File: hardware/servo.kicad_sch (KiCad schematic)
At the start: 3 parts, among them J701 Conn_02x03_Odd_Even

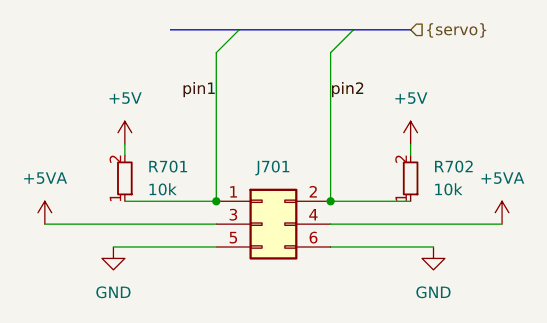
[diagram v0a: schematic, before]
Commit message: update board file, made similar to OS solenoid decoder
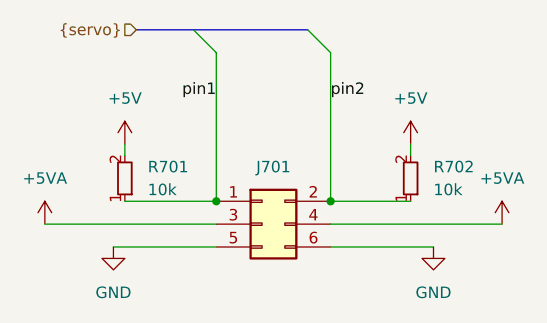
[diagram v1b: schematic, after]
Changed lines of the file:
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@@
 	)
 	(bus_entry
-		(at 149.86 69.85)
-		(size -2.54 2.54)
+		(at 132.08 69.85)
+		(size 2.54 2.54)
 		(stroke
 			(width 0)
@@
 	)
 	(bus_entry
-		(at 137.16 69.85)
-		(size -2.54 2.54)
+		(at 144.78 69.85)
+		(size 2.54 2.54)
 		(stroke
 			(width 0)
@@
 	(bus
 		(pts
-			(xy 137.16 69.85) (xy 149.86 69.85)
+			(xy 144.78 69.85) (xy 132.08 69.85)
 		)
 		(stroke
@@
 		(pts
 			(xy 115.57 91.44) (xy 134.62 91.44)
-		)
-		(stroke
-			(width 0)
-			(type default)
-		)
-	)
-	(bus
-		(pts
-			(xy 129.54 69.85) (xy 137.16 69.85)
 		)
 		(stroke
@@
 	(bus
 		(pts
-			(xy 149.86 69.85) (xy 156.21 69.85)
+			(xy 132.08 69.85) (xy 125.73 69.85)
 		)
 		(stroke
@@
 	(hierarchical_label "{servo}"
 		(shape input)
-		(at 156.21 69.85 0)
+		(at 125.73 69.85 180)
 		(fields_autoplaced yes)
 		(effects
@@
 				(size 1.27 1.27)
 			)
-			(justify left)
+			(justify right)
 		)
 	)
